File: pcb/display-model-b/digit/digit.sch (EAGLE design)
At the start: 53 parts, among them J1 SOLDER_JUMPER_3, J2 SOLDER_JUMPER_3, J3 SOLDER_JUMPER_3, Q1 MMBT3904, Q2 MMBT3904, Q3 MMBT3904, Q4 MMBT3904, Q5 MMBT3904, Q6 MMBT3904, Q7 MMBT3904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

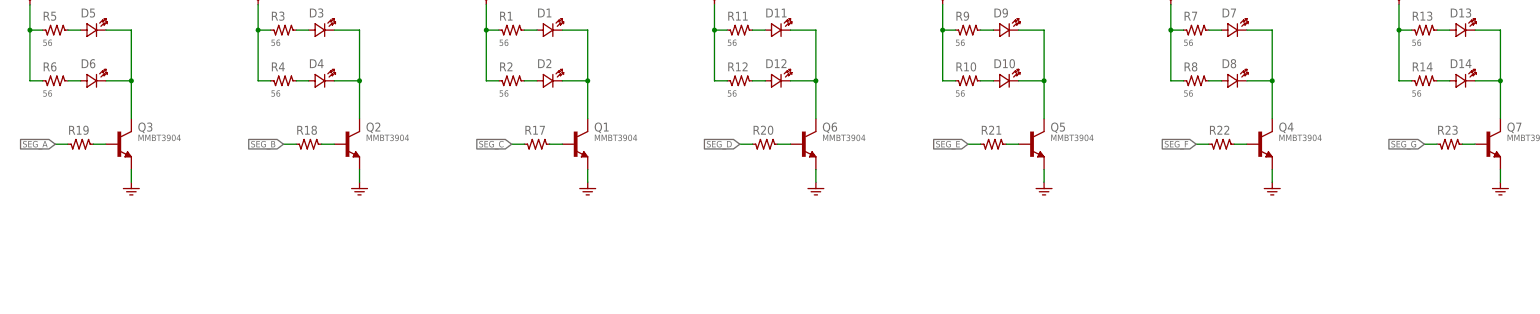
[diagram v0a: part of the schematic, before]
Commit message: Added Model B drawings
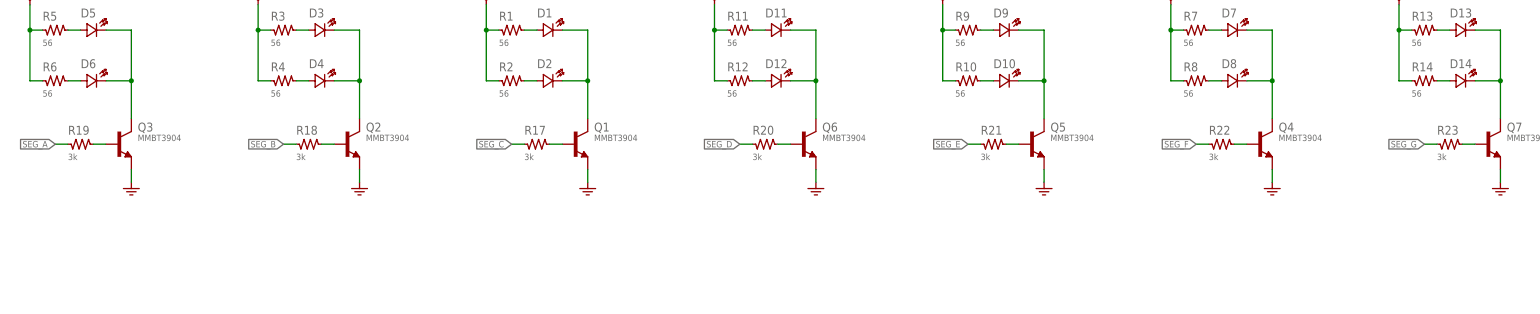
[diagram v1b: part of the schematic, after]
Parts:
- R17, R18, R19, R20, R21, R22, R23: value (none) -> 3k
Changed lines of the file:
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@@
 <attribute name="DOC_REV" value="A"/>
 <attribute name="DOC_SUBTITLE" value=" "/>
-<attribute name="DOC_TITLE" value="Display (Model B) - Segment PCB"/>
-<attribute name="PROJECT_NAME" value="Alarm Clock"/>
+<attribute name="DOC_TITLE" value="7 Segment display"/>
+<attribute name="PROJECT_NAME" value="Alarm Clock (Model B)"/>
 </attributes>
 <variantdefs>
@@
 <part name="R16" library="Passive" deviceset="RES" device="-0603" value="N/A"/>
 <part name="SUPPLY8" library="Power" deviceset="3.3V" device=""/>
-<part name="R17" library="Passive" deviceset="RES" device="-0603"/>
-<part name="R18" library="Passive" deviceset="RES" device="-0603">
-<attribute name="DESCRIPTION" value="{DESCRIPTION} - SMT 0603 - {VALUE}"/>
-<attribute name="PACKAGE" value="SMT 0603"/>
-<attribute name="PART" value=""/>
-</part>
-<part name="R19" library="Passive" deviceset="RES" device="-0603">
-<attribute name="DESCRIPTION" value="{DESCRIPTION} - SMT 0603 - {VALUE}"/>
-<attribute name="PACKAGE" value="SMT 0603"/>
-<attribute name="PART" value=""/>
-</part>
-<part name="R20" library="Passive" deviceset="RES" device="-0603">
-<attribute name="DESCRIPTION" value="{DESCRIPTION} - SMT 0603 - {VALUE}"/>
-<attribute name="PACKAGE" value="SMT 0603"/>
-<attribute name="PART" value=""/>
-</part>
-<part name="R21" library="Passive" deviceset="RES" device="-0603">
-<attribute name="DESCRIPTION" value="{DESCRIPTION} - SMT 0603 - {VALUE}"/>
-<attribute name="PACKAGE" value="SMT 0603"/>
-<attribute name="PART" value=""/>
-</part>
-<part name="R22" library="Passive" deviceset="RES" device="-0603">
-<attribute name="DESCRIPTION" value="{DESCRIPTION} - SMT 0603 - {VALUE}"/>
-<attribute name="PACKAGE" value="SMT 0603"/>
-<attribute name="PART" value=""/>
-</part>
-<part name="R23" library="Passive" deviceset="RES" device="-0603">
-<attribute name="DESCRIPTION" value="{DESCRIPTION} - SMT 0603 - {VALUE}"/>
-<attribute name="PACKAGE" value="SMT 0603"/>
+<part name="R17" library="Passive" deviceset="RES" device="-0603" value="3k"/>
+<part name="R18" library="Passive" deviceset="RES" device="-0603" value="3k">
+<attribute name="DESCRIPTION" value="{DESCRIPTION} - SMT 0603 - {VALUE}"/>
+<attribute name="PACKAGE" value="SMT 0603"/>
+<attribute name="PART" value=""/>
+</part>
+<part name="R19" library="Passive" deviceset="RES" device="-0603" value="3k">
+<attribute name="DESCRIPTION" value="{DESCRIPTION} - SMT 0603 - {VALUE}"/>
+<attribute name="PACKAGE" value="SMT 0603"/>
+<attribute name="PART" value=""/>
+</part>
+<part name="R20" library="Passive" deviceset="RES" device="-0603" value="3k">
+<attribute name="DESCRIPTION" value="{DESCRIPTION} - SMT 0603 - {VALUE}"/>
+<attribute name="PACKAGE" value="SMT 0603"/>
+<attribute name="PART" value=""/>
+</part>
+<part name="R21" library="Passive" deviceset="RES" device="-0603" value="3k">
+<attribute name="DESCRIPTION" value="{DESCRIPTION} - SMT 0603 - {VALUE}"/>
+<attribute name="PACKAGE" value="SMT 0603"/>
+<attribute name="PART" value=""/>
+</part>
+<part name="R22" library="Passive" deviceset="RES" device="-0603" value="3k">
+<attribute name="DESCRIPTION" value="{DESCRIPTION} - SMT 0603 - {VALUE}"/>
+<attribute name="PACKAGE" value="SMT 0603"/>
+<attribute name="PART" value=""/>
+</part>
+<part name="R23" library="Passive" deviceset="RES" device="-0603" value="3k">
+<attribute name="DESCRIPTION" value="{DESCRIPTION} - SMT 0603 - {VALUE}"/>
+<attribute name="PACKAGE" value="SMT 0603"/>
